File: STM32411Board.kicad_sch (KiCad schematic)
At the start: 18 parts, among them J1 Conn_02x10_Odd_Even, U1 STM32F411CEUx, Y1 25Mhz 8pF, Y2 32kHz 8pF

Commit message: update
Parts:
- removed C6: 100n, Capacitor_SMD:C_0805_2012Metric_Pad1.18x1.45mm_HandSolder, symbol Device:C
- added C14: 1u, Capacitor_SMD:C_0603_1608Metric, symbol Device:C_Polarized
- C1, C10, C11, C12, C13, C8: footprint (none) -> Capacitor_SMD:C_0603_1608Metric
- C2, C3, C4, C5, C7: footprint Capacitor_SMD:C_0805_2012Metric_Pad1.18x1.45mm_HandSolder -> Capacitor_SMD:C_0603_1608Metric
- C9: value C -> 4u7; footprint Capacitor_SMD:CP_Elec_4x3 -> Capacitor_SMD:C_0603_1608Metric
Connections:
- net +3V3: now also C14.1
- net GND: now also C14.2
- net osc32_in: now also C13.1, Y2.3
- net osc32_out: now also C12.1, Y2.1; no longer C13.1, Y2.3
- net osc_in: now also C11.1, Y1.3; no longer C10.1, Y1.1
- net osc_out: now also C10.1, Y1.1; no longer C11.1, Y1.3

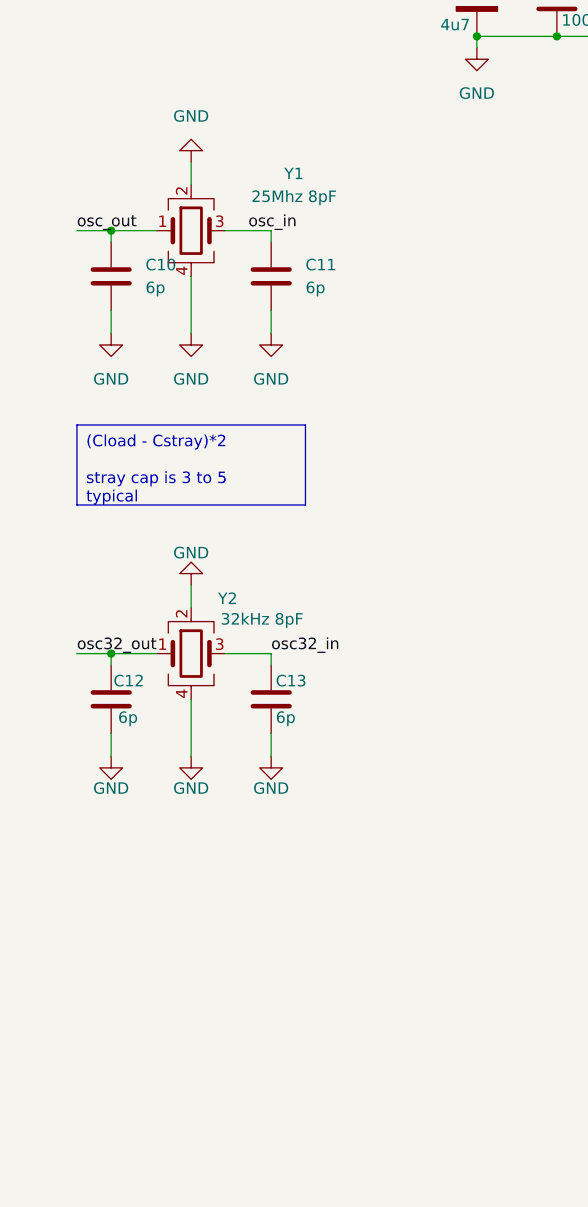
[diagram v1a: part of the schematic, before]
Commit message: updated crystal
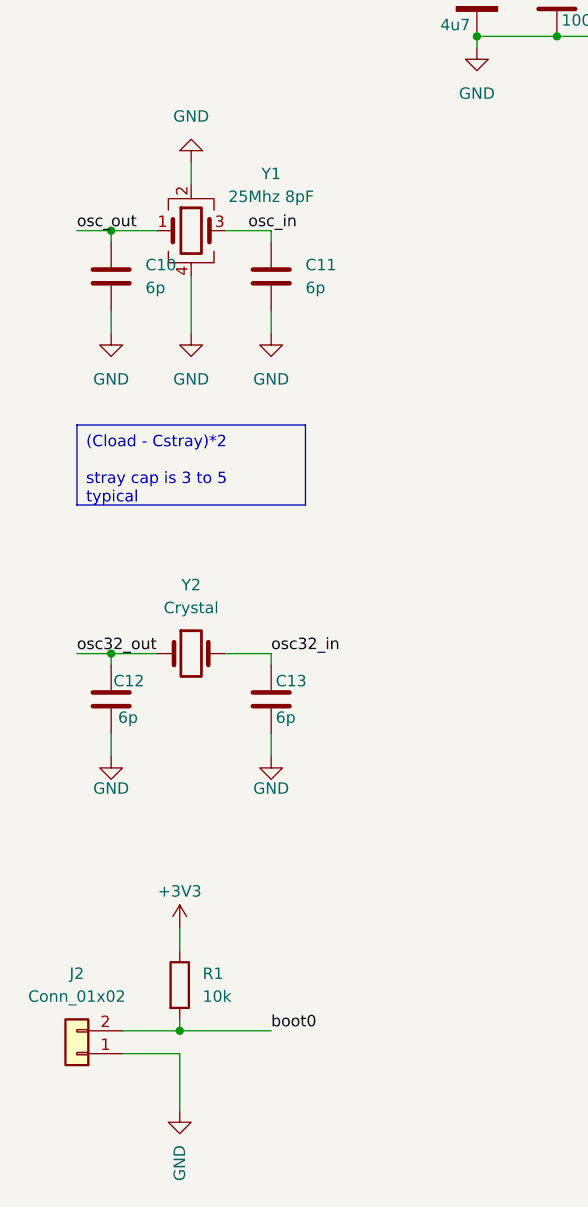
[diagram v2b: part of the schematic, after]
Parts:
- removed Y2: 32kHz 8pF, Crystal:Crystal_SMD_3225-4Pin_3.2x2.5mm, symbol Device:Crystal_GND24
- added J2: Conn_01x02, Connector_PinHeader_2.54mm:PinHeader_1x02_P2.54mm_Vertical, symbol Connector_Generic:Conn_01x02
- added R1: 10k, Resistor_SMD:R_0805_2012Metric, symbol Device:R
- added Y2: Crystal, Crystal:Crystal_SMD_3215-2Pin_3.2x1.5mm, symbol Device:Crystal
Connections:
- net +3V3: now also R1.1
- net GND: now also J2.1 (Pin_1)
- net boot0: now also J2.2 (Pin_2), R1.2
- net osc32_in: now also Y2.2
- net osc32_out: now also Y2.1
